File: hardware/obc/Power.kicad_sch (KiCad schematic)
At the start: 68 parts, among them Q1 IRLML2803, Q14 IRF7406PbF, Q2 MBT2222ADW1T1, Q3 MBT2222ADW1T1, U10 BQ25886RGER, U21 TPS7A4501DCQT, U4 ADM1176-1ARMZ-R7, U5 TPS54226PWPRPWP14_2P31X2P46-L, U6 LTC4121

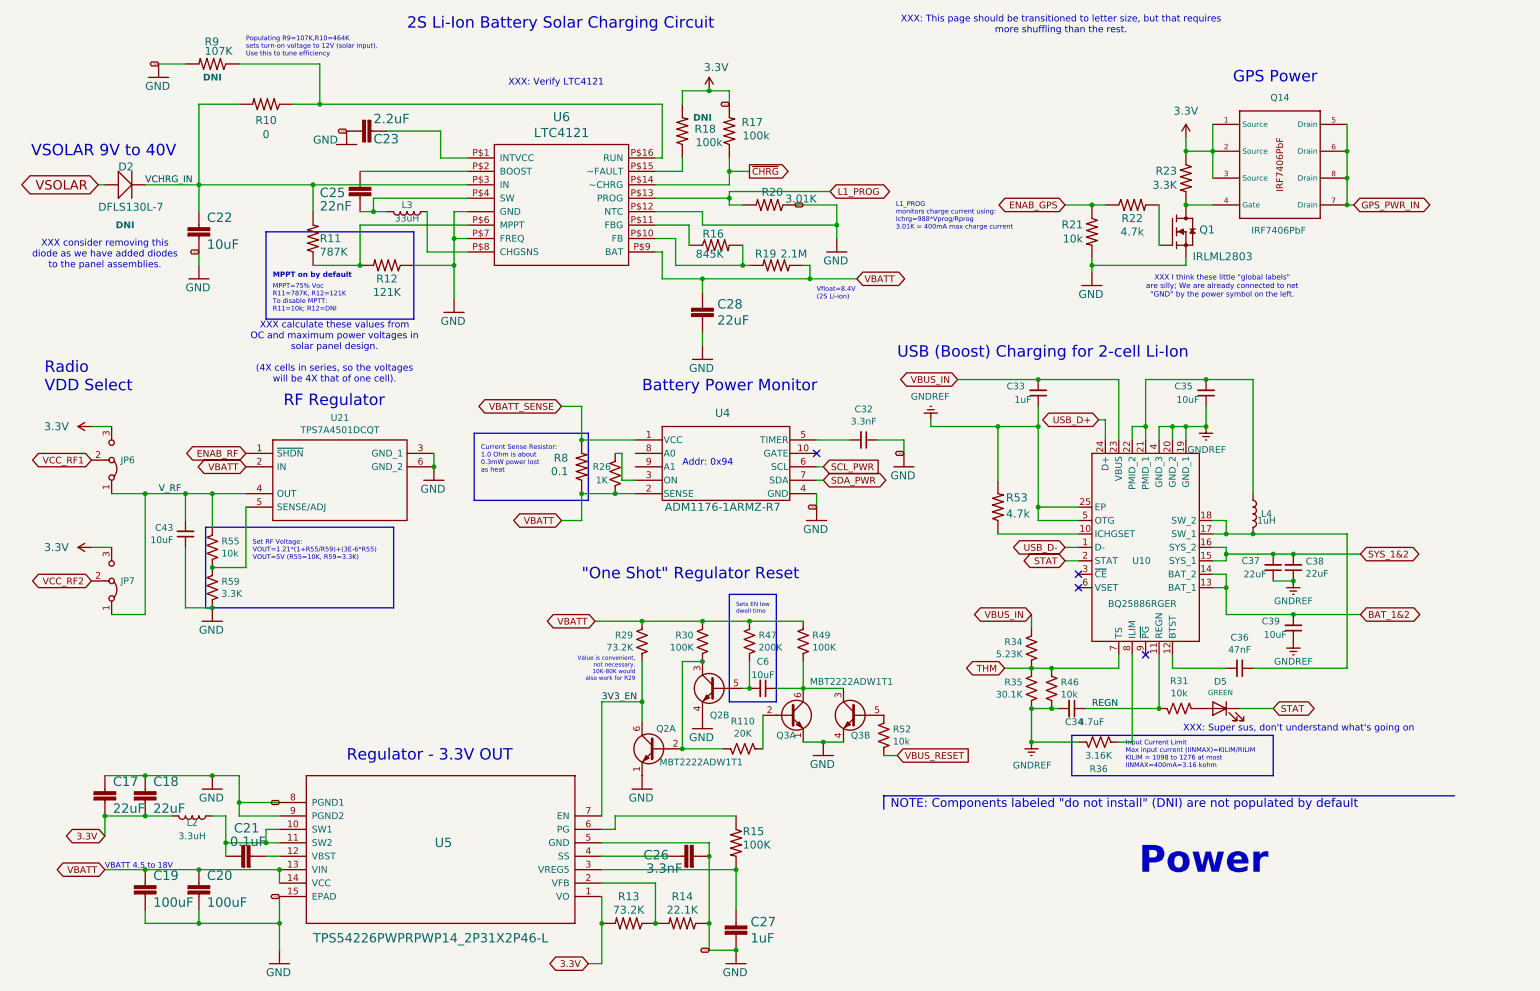
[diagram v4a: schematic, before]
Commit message: obc: footprint editing and schematic revision
Added GPS21+ and edited inductor footprints. Edited schematic circuitry and re-annotated schematic components.
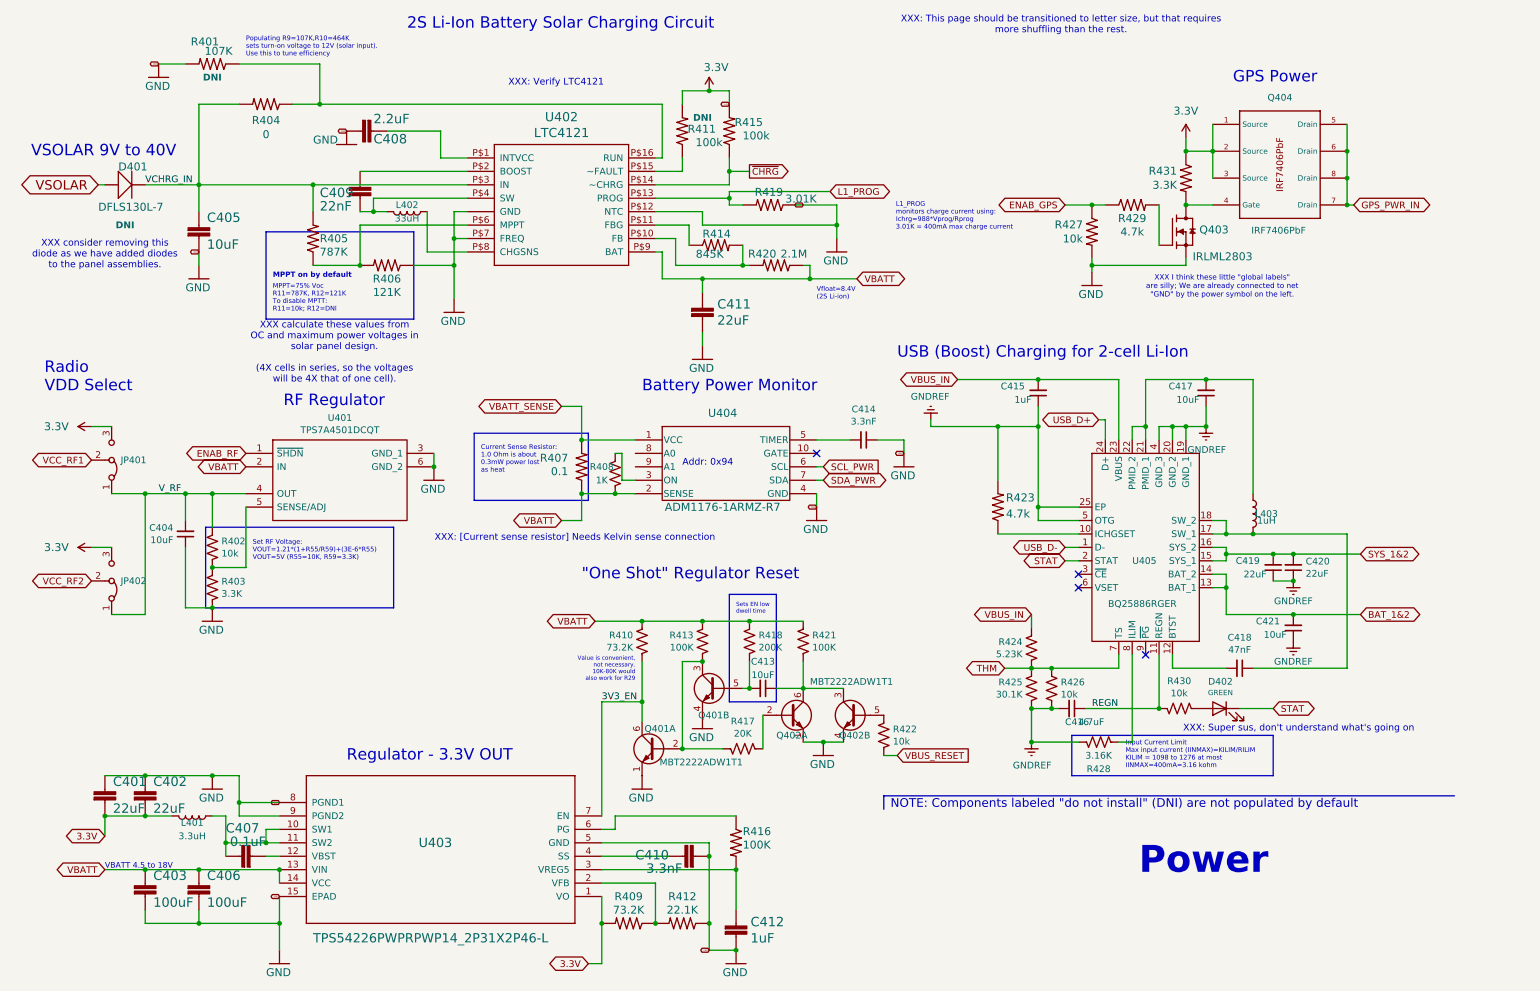
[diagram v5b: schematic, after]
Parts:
- R407: renamed from R8; LCSC (none) -> C165698; Notes Cannot find. -> (none)
- renumbered C17 to C401, C18 to C402, C19 to C403, C43 to C404, C22 to C405, C20 to C406, C21 to C407, C23 to C408, C25 to C409, C26 to C410, C28 to C411, C27 to C412, C6 to C413, C32 to C414, C33 to C415, C34 to C416, C35 to C417, C36 to C418, C37 to C419, C38 to C420, C39 to C421, D2 to D401, D5 to D402, JP6 to JP401, JP7 to JP402, L2 to L401, L3 to L402, L4 to L403, Q2 to Q401, Q3 to Q402, Q1 to Q403, Q14 to Q404, R9 to R401, R55 to R402, R59 to R403, R10 to R404, R11 to R405, R12 to R406, R26 to R408, R13 to R409, R29 to R410, R18 to R411, R14 to R412, R30 to R413, R16 to R414, R17 to R415, R15 to R416, R110 to R417, R47 to R418, R20 to R419, R19 to R420, R49 to R421, R52 to R422, R53 to R423, R34 to R424, R35 to R425, R46 to R426, R21 to R427, R36 to R428, R22 to R429, R31 to R430, R23 to R431, U21 to U401, U6 to U402, U5 to U403, U4 to U404, U10 to U405
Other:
- note added: "XXX: [Current sense resistor] Needs Kelvin sense connection"

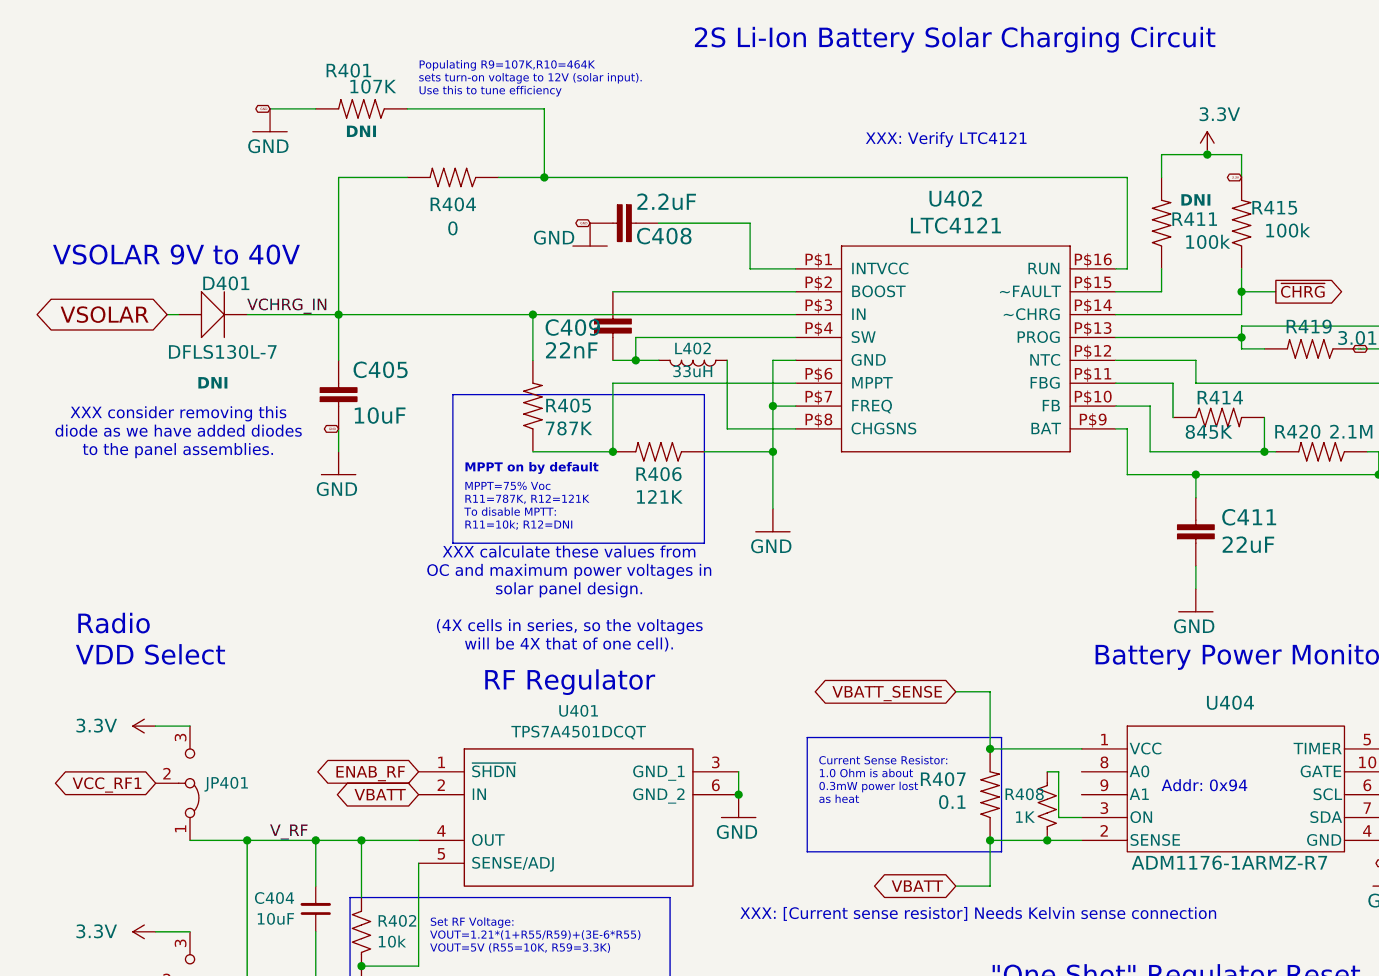
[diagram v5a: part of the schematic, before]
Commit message: obc: BOM editing
Edited the DNI status of several components to be more reflective of our obc setup plans.
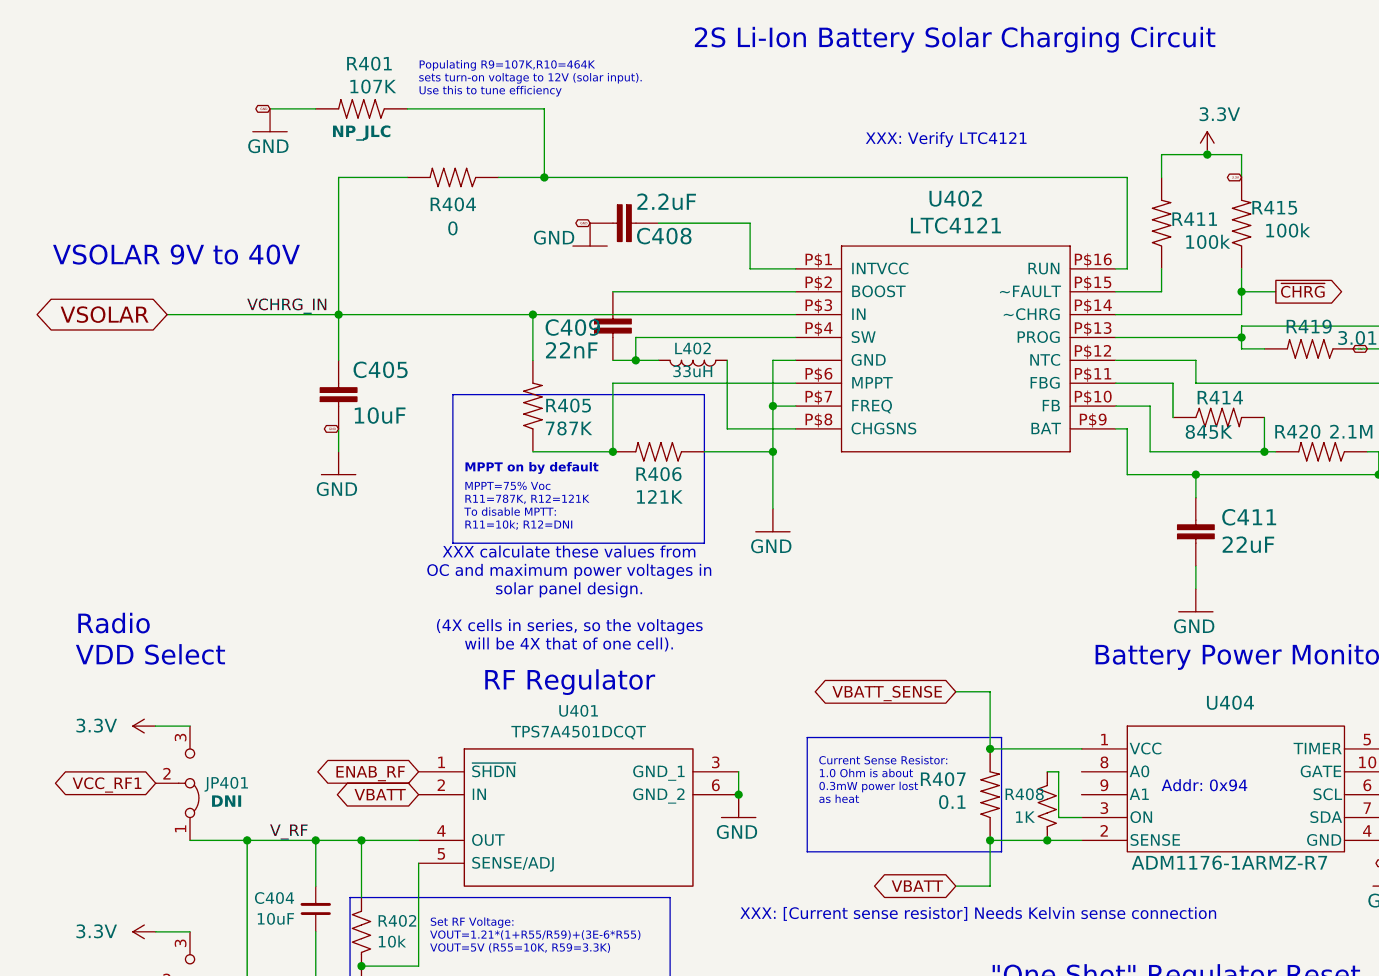
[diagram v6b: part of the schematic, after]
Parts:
- removed D401: DFLS130L-7, mainboard:PWRDI-123, symbol mainboard:DFLS130L
- JP401, JP402: Notes Output voltage for radio. -> (none)
- R401: DNI DNI -> NP_JLC; LCSC C4028352 -> (none); Manufacturer_Name Vishay Intertech -> (none); Manufacturer_Part_Number CRCW0603107KFKEA -> (none)
- R411: DNI DNI -> (none)
- U404: Notes Consigned parts to JLCPCB. -> (none)
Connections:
- net VCHRG_IN is gone; now on net VSOLAR: C405.1, R404.2, R405.2, U402.P$3 (IN)
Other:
- note removed: "XXX consider removing this diode as we have added diodes to the panel assemblies."
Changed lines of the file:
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@@
 	(wire
 		(pts
-			(xy 29.21 46.99) (xy 27.94 46.99)
+			(xy 27.94 46.99) (xy 46.99 46.99)
 		)
 		(stroke
@@
 	(wire
 		(pts
-			(xy 36.83 46.99) (xy 46.99 46.99)
-		)
-		(stroke
-			(width 0)
-			(type default)
-		)
-	)
-	(wire
-		(pts
 			(xy 147.32 31.75) (xy 147.32 29.21)
 		)
@@
 		)
 	)
-	(text "XXX consider removing this\ndiode as we have added diodes\nto the panel assemblies."
-		(exclude_from_sim no)
-		(at 29.21 60.198 0)
-		(effects
-			(font
-				(size 1.27 1.27)
-			)
-		)
-	)
 	(label "V_RF"
 		(at 39.37 105.41 0)
@@
 	)
 	(symbol
-		(lib_id "mainboard:DFLS130L")
-		(at 31.75 46.99 0)
-		(unit 1)
-		(exclude_from_sim no)
-		(in_bom yes)
-		(on_board yes)
-		(dnp no)
-		(property "Reference" "D401"
-			(at 31.75 44.45 0)
-			(effects
-				(font
-					(size 1.4986 1.4986)
-				)
-				(justify left bottom)
-			)
-		)
-		(property "Value" "DFLS130L-7"
-			(at 27.94 52.07 0)
-			(effects
-				(font
-					(size 1.4986 1.4986)
-				)
-				(justify left bottom)
-			)
-		)
-		(property "Footprint" "mainboard:PWRDI-123"
-			(at 31.75 46.99 0)
-			(effects
-				(font
-					(size 1.27 1.27)
-				)
-				(hide yes)
-			)
-		)
-		(property "Datasheet" "https://www.diodes.com/assets/Datasheets/ds30492.pdf"
-			(at 31.75 46.99 0)
-			(effects
-				(font
-					(size 1.27 1.27)
-				)
-				(hide yes)
-			)
-		)
-		(property "Description" "Schottky Diode - 30V 310mV@1A 1A Power-DI-123"
-			(at 31.75 46.99 0)
-			(effects
-				(font
-					(size 1.27 1.27)
-				)
-				(hide yes)
-			)
-		)
-		(property "Flight" "DFLS130L-7"
-			(at 31.75 46.99 0)
-			(effects
-				(font
-					(size 1.27 1.27)
-				)
-				(hide yes)
-			)
-		)
-		(property "Manufacturer_Name" "Diodes Incorporated"
-			(at 31.75 46.99 0)
-			(effects
-				(font
-					(size 1.27 1.27)
-				)
-				(hide yes)
-			)
-		)
-		(property "Manufacturer_Part_Number" "DFLS130L-7"
-			(at 31.75 41.91 0)
-			(effects
-				(font
-					(size 1.27 1.27)
-				)
-				(hide yes)
-			)
-		)
-		(property "Proto" "DFLS130L"
-			(at 31.75 46.99 0)
-			(effects
-				(font
-					(size 1.27 1.27)
-				)
-				(hide yes)
-			)
-		)
-		(property "DNI" "DNI"
-			(at 33.02 54.61 0)
-			(effects
-				(font
-					(size 1.27 1.27)
-					(bold yes)
-				)
-			)
-		)
-		(property "LCSC" "C110493"
-			(at 31.75 46.99 0)
-			(effects
-				(font
-					(size 1.27 1.27)
-				)
-				(hide yes)
-			)
-		)
-		(property "Notes" ""
-			(at 31.75 46.99 0)
-			(effects
-				(font
-					(size 1.27 1.27)
-				)
-				(hide yes)
-			)
-		)
-		(property "Height" ""
-			(at 31.75 46.99 0)
-			(effects
-				(font
-					(size 1.27 1.27)
-				)
-				(hide yes)
-			)
-		)
-		(property "Mouser Part Number" ""
-			(at 31.75 46.99 0)
-			(effects
-				(font
-					(size 1.27 1.27)
-				)
-				(hide yes)
-			)
-		)
-		(property "Mouser Price/Stock" ""
-			(at 31.75 46.99 0)
-			(effects
-				(font
-					(size 1.27 1.27)
-				)
-				(hide yes)
-			)
-		)
-		(pin "A"
-		)
-		(pin "C"
-		)
-		(instances
-			(project "mainboard"
-				(path "/e3ac22ea-6806-4807-a025-571315789c25/00000000-0000-0000-0000-00005cec5dde"
-					(reference "D401")
-					(unit 1)
-				)
-			)
-		)
-	)
-	(symbol
 		(lib_id "mainboard:R-US_R0603")
 		(at 138.43 186.69 180)
@@
 			)
 		)
-		(property "DNI" "DNI"
+		(property "DNI" ""
 			(at 142.24 34.29 90)
 			(effects
@@
 			)
 		)
-		(property "Notes" "Consigned parts to JLCPCB."
+		(property "Notes" ""
 			(at 127 81.28 0)
 			(effects
@@
 			)
 		)
-		(property "Description" "Vertical Header - 0.1in (2.54mm)"
+		(property "Description" "Radio Output Vdd Select"
 			(at 34.7218 99.06 0)
 			(effects
@@
 		)
 		(property "DNI" "DNI"
-			(at 34.7218 99.06 0)
+			(at 34.544 101.092 90)
 			(effects
 				(font
 					(size 1.27 1.27)
+					(bold yes)
 				)
-				(hide yes)
 			)
 		)
@@
 			)
 		)
-		(property "Notes" "Output voltage for radio."
+		(property "Notes" ""
 			(at 30.48 99.06 0)
 			(effects
@@
 			)
 		)
-		(property "Description" "Vertical Header - 0.1in (2.54mm)"
+		(property "Description" "Radio Output Vdd Select"
 			(at 34.7218 121.92 0)
 			(effects
@@
 			)
 		)
-		(property "Notes" "Output voltage for radio."
+		(property "Notes" ""
 			(at 30.48 121.92 0)
 			(effects
@@
 		(dnp no)
 		(property "Reference" "R401"
-			(at 50.8 19.05 0)
+			(at 53.086 18.288 0)
 			(effects
 				(font
@@
 			)
 		)
-		(property "DNI" "DNI"
+		(property "DNI" "NP_JLC"
 			(at 49.53 26.67 0)
 			(effects
@@
 			)
 		)
-		(property "LCSC" "C4028352"
+		(property "LCSC" ""
 			(at 49.53 24.13 0)
 			(effects
@@
 			)
 		)
-		(property "Manufacturer_Name" " Vishay Intertech"
+		(property "Manufacturer_Name" ""
 			(at 49.53 24.13 0)
 			(effects
@@
 			)
 		)
-		(property "Manufacturer_Part_Number" " CRCW0603107KFKEA"
+		(property "Manufacturer_Part_Number" ""
 			(at 49.53 24.13 0)
 			(effects

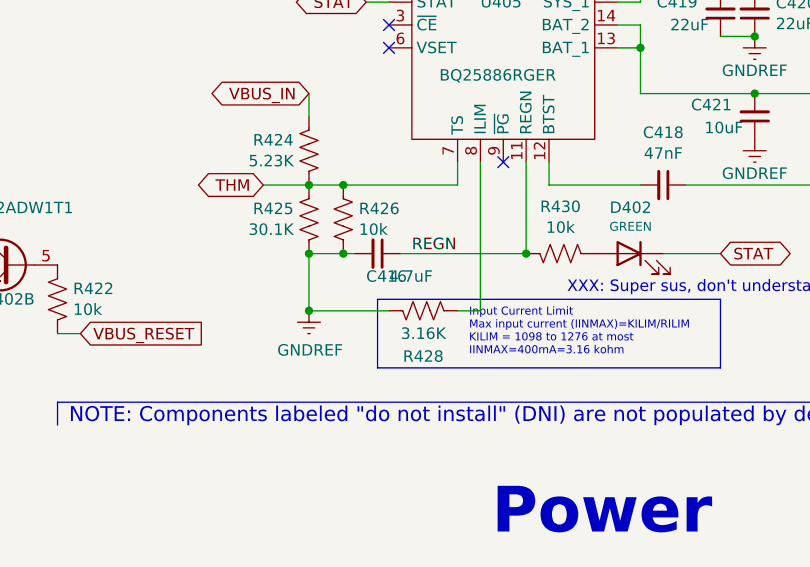
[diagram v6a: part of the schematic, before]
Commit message: obc: formal placement and 3D models entered
Placed components of onto board, orienting them for ease of trace creation. Entered 3D models of footprints into KiCad for design verification and aesthetics.
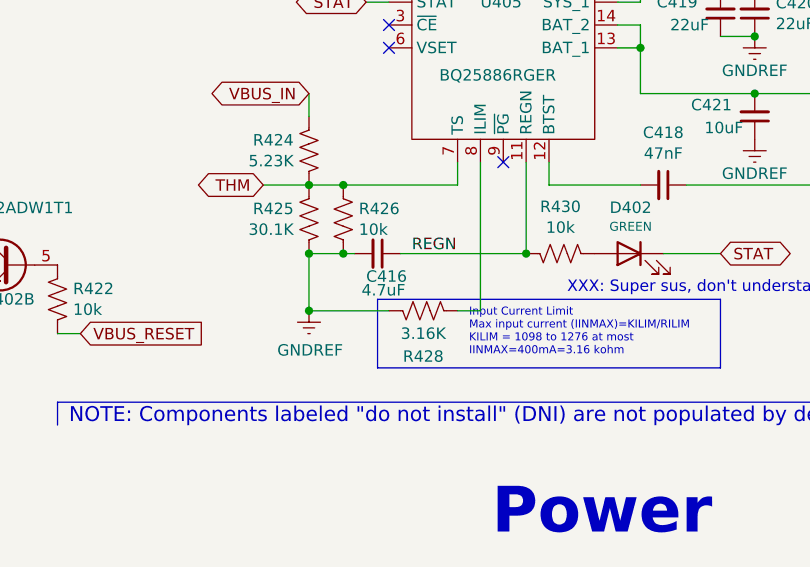
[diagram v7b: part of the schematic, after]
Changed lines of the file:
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@@
 		)
 		(property "Value" "4.7uF"
-			(at 213.36 148.59 90)
+			(at 210.312 150.114 90)
 			(effects
 				(font

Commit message: obc: various changes from design review
- change 1008 inductor footprint to one from kicad library
- change 'default class' design rules to match board design rules
- back-annotate from layout to board
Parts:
- L403: footprint SSE_Footprints:Murata_1008_2.5x2.0mm -> Inductor_SMD:L_1008_2520Metric
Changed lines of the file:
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@@
 			)
 		)
-		(property "Footprint" "SSE_Footprints:Murata_1008_2.5x2.0mm"
+		(property "Footprint" "Inductor_SMD:L_1008_2520Metric"
 			(at 246.38 109.22 0)
 			(effects
